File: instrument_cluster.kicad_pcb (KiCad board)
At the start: 2 copper layers, 99.1 x 45.7 mm, 80 parts, among them J1 Conn_02x16_Top_Bottom, J2 Conn_02x16_Top_Bottom, J3 USB mini-B SMD, J4 NOT_FITTED_SWD_Conn_01x04_Male, J5 54819-0572, J6 NOT_FITTED_SWD_Conn_01x04_Male, U1 LM2575S-5.0_NOPB, U10 74HC4050D, U11 TJA1040T, U12 TJA1040T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

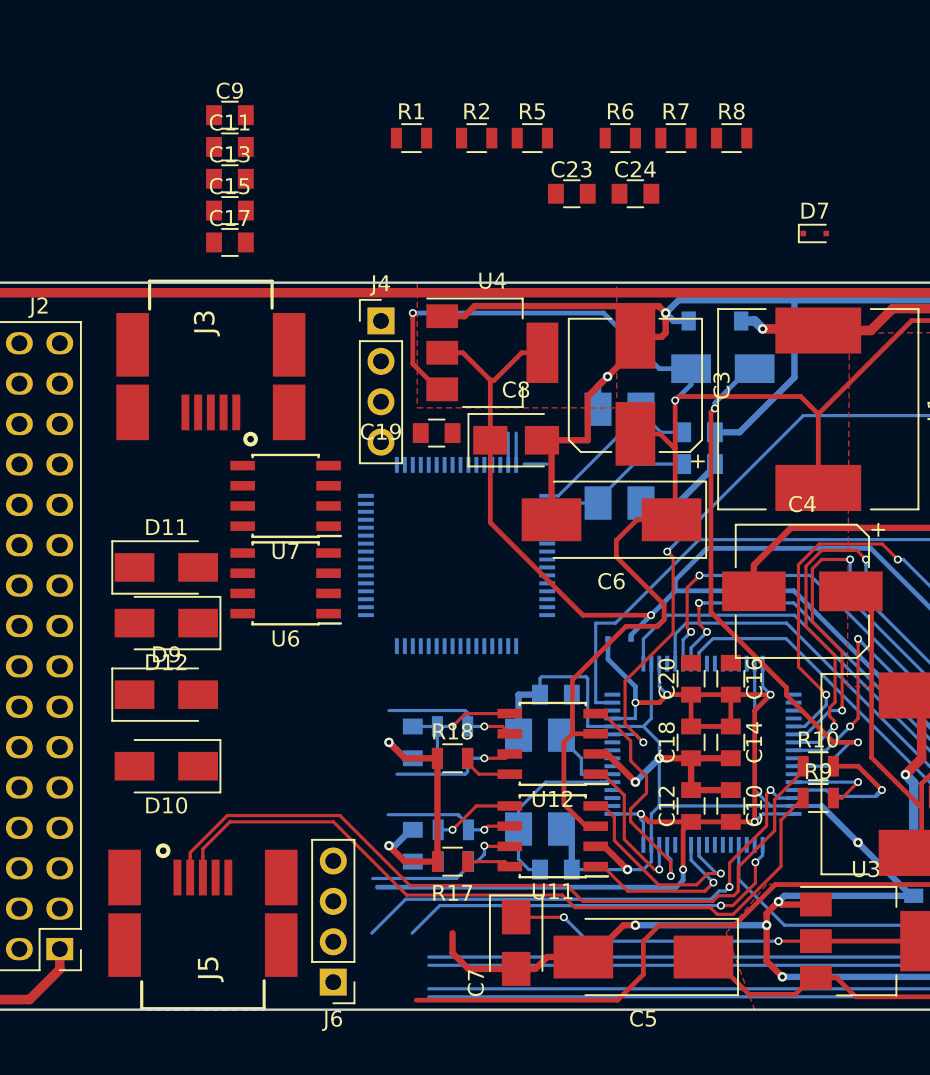
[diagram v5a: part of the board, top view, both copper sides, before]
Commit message: add resistor on can STB pin module A
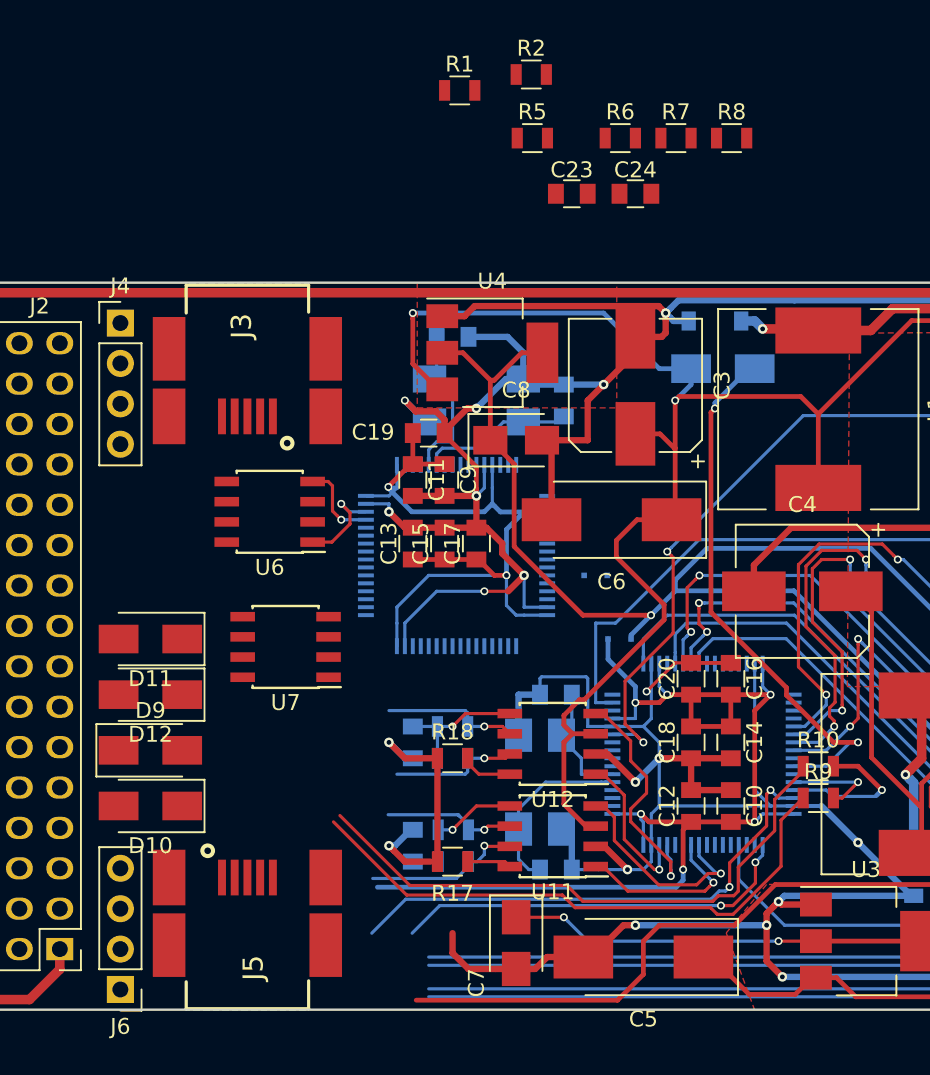
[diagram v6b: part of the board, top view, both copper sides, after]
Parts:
- D7: moved to B.Cu
- moved C9 26.6 mm to (138.5, 97.5), turned to 270 degrees
- moved C13 25.7 mm to (136.5, 101.5), turned to 90 degrees
- moved D7 25.5 mm to (148.0, 103.5)
- moved C15 24.9 mm to (138.5, 101.5), turned to 90 degrees
- moved C17 24.5 mm to (140.5, 101.5), turned to 90 degrees
- moved C11 23.9 mm to (136.5, 97.5), turned to 270 degrees
- moved C21 16.6 mm to (139.0, 88.5)
- moved J4 16.4 mm to (118.1, 87.6)
- moved J6 13.4 mm to (118.1, 129.5)
- moved Y1 9.66 mm to (140.5, 92.5), turned to 0 degrees
- moved U7 9.50 mm to (128.5, 108.0)
- moved C22 9.39 mm to (146.0, 92.5), turned to 90 degrees
- moved R2 5.27 mm to (143.9, 72.0)
- moved D11 4.61 mm to (120.0, 107.5), turned to 180 degrees
- moved D12 4.61 mm to (120.0, 111.0)
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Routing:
- net GND: track 402.9 -> 452.2 mm, vias 20 -> 27
- net /+3V3_STM-A: track 0.83 -> 49.6 mm, vias 0 -> 2
- net Net-(J5-Pad2): track 49.1 -> 37.1 mm
- net Net-(J5-Pad3): track 47.4 -> 36.7 mm
- net /Module A (2can_filter)/CAN1_TX: track 0.00 -> 6.07 mm, vias 0 -> 1
- net /Module A (2can_filter)/CAN1_RX: track 0.00 -> 5.27 mm, vias 0 -> 1
- net (no net): track 4.35 -> 0.00 mm
- net Net-(C22-Pad1): track 8.15 -> 9.87 mm
- net Net-(U5-Pad2): track 1.55 -> 0.00 mm
- net Net-(C21-Pad1): track 11.4 -> 10.1 mm
- net /+5V_CAN-B: track 99.9 -> 99.4 mm

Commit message: TODO swd module A, anti-theft
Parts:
- added R3: 10k, Resistors_SMD:R_0805, F.Cu at (121.0, 100.0)
- added R4: 10k, Resistors_SMD:R_0805, F.Cu at (130.5, 108.5)
- C23, C24, D10, D11, D12, D9, R5, R6, R7, R8: moved to B.Cu
- moved R8 42.1 mm to (127.0, 106.0), turned to 90 degrees
- moved R7 38.5 mm to (129.0, 106.0), turned to 270 degrees
- moved R2 37.1 mm to (137.5, 108.5), turned to 90 degrees
- moved C24 36.7 mm to (128.0, 108.5)
- moved R6 36.0 mm to (121.0, 98.0)
- moved R1 35.5 mm to (139.5, 108.5), turned to 90 degrees
- moved C23 34.1 mm to (118.5, 99.0), turned to 90 degrees
- moved R5 33.2 mm to (121.0, 100.0)
- moved U7 3.58 mm to (130.3, 104.9)
- moved R9 2.92 mm to (160.5, 120.0), turned to 90 degrees
- moved R10 2.24 mm to (160.0, 114.5)
- moved D10 1.00 mm to (120.0, 117.0)
- moved D11 1.00 mm to (120.0, 106.5), turned to 0 degrees
- moved D12 1.00 mm to (120.0, 110.0)
- moved D9 1.00 mm to (120.0, 113.5)
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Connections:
- U6 pad 8: GND -> Net-(R3-Pad1)
- U7 pad 8: GND -> Net-(R4-Pad1)
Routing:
- net GND: track 452.2 -> 582.7 mm, vias 27 -> 34
- net /USB_Vbus-A: track 41.2 -> 105.0 mm, vias 0 -> 2
- net /MS_CAN_H: track 74.9 -> 132.8 mm, vias 1 -> 6
- net /MS_CAN_L: track 81.5 -> 136.5 mm, vias 1 -> 7
- net /HS_CAN_H: track 73.6 -> 125.8 mm, vias 1 -> 6
- net /HS_CAN_L: track 72.9 -> 125.1 mm, vias 1 -> 6
- net /USB_Vbus-B: track 34.2 -> 81.4 mm, vias 2 -> 4
- net Net-(J3-Pad3): track 0.00 -> 28.3 mm, vias 0 -> 2
- net /ANTI-THEFT: track 17.6 -> 39.4 mm
- net Net-(J3-Pad2): track 0.00 -> 21.8 mm
- net /+3V3_STM-B: track 72.2 -> 91.6 mm
- net /Module B (2can_filter+extra)/SWCLK: track 25.5 -> 44.5 mm
- net /Module B (2can_filter+extra)/SWDIO: track 32.5 -> 49.7 mm
- net /+5V_CAN-A: track 143.0 -> 153.4 mm
- net Net-(C24-Pad2): track 0.00 -> 9.89 mm, vias 0 -> 1
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
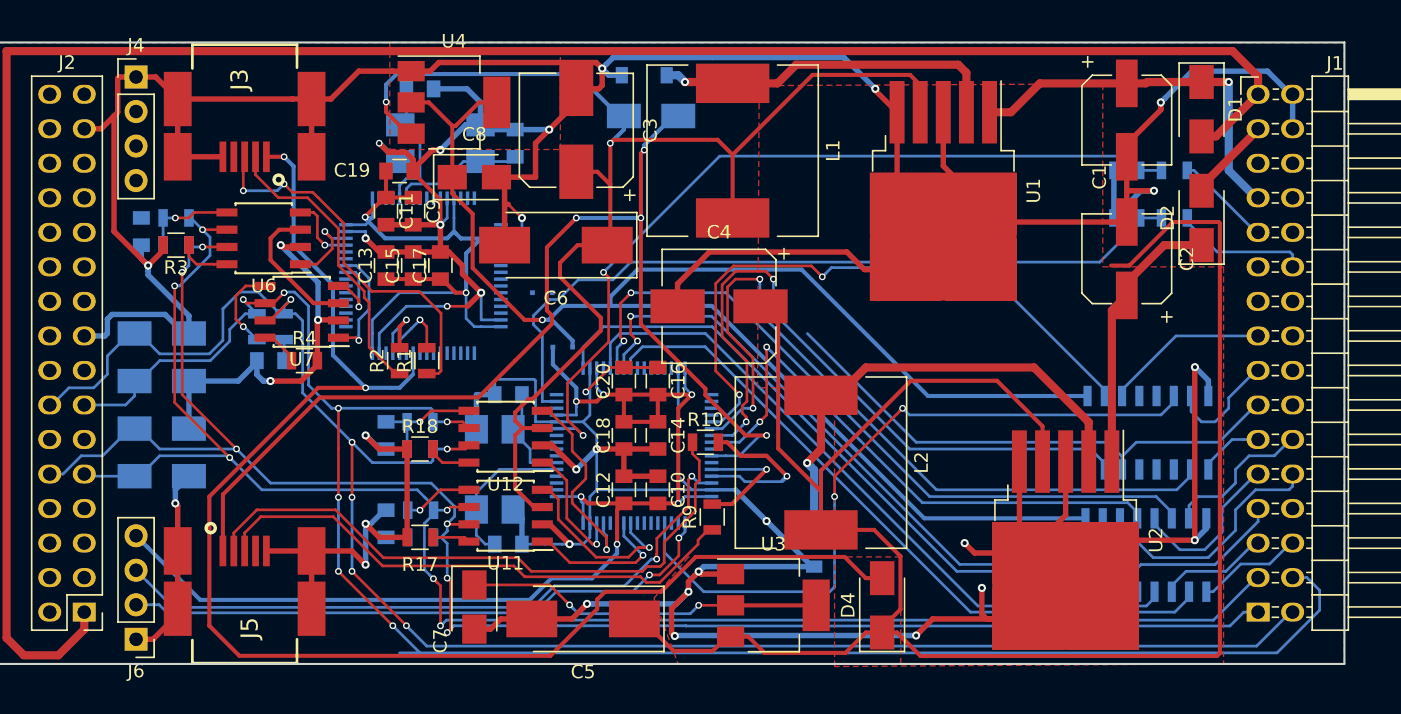
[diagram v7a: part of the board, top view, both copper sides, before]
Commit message: pcb tracing finish
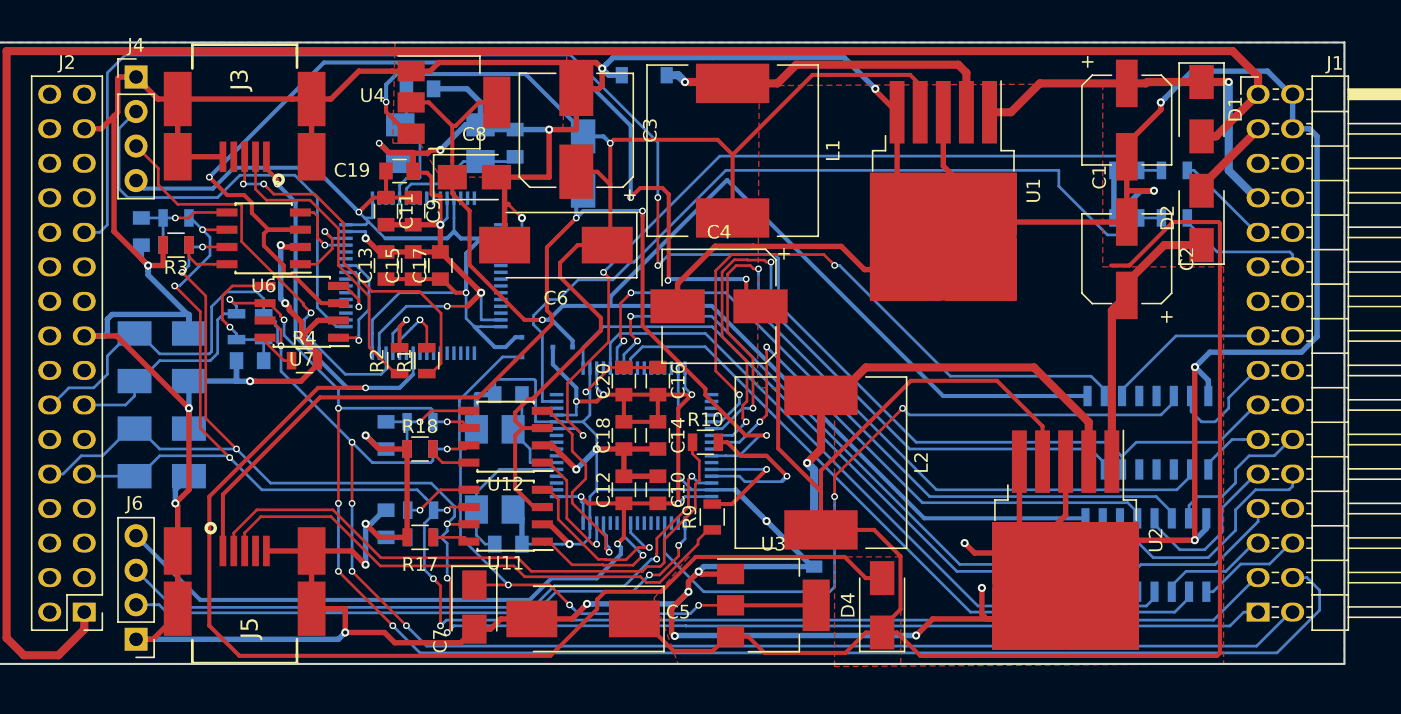
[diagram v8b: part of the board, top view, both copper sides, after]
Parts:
- moved D3 6.10 mm to (151.0, 94.0), turned to 270 degrees
- moved D7 4.27 mm to (146.5, 107.5), turned to 270 degrees
- moved C24 1.50 mm to (126.5, 108.5)
- moved R7 1.50 mm to (127.5, 106.0)
- moved R8 1.50 mm to (125.5, 106.0)
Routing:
- net GND: track 582.7 -> 665.1 mm, vias 34 -> 36
- net /ANTI-THEFT: track 39.4 -> 121.0 mm, vias 0 -> 2
- net /+5V_CAN-A: track 153.4 -> 222.6 mm, vias 0 -> 4
- net /Module A (2can_filter)/SWCLK: track 0.00 -> 33.2 mm
- net /Module A (2can_filter)/SWDIO: track 0.00 -> 30.6 mm, vias 0 -> 1
- net /+3V3_STM-A: track 49.6 -> 73.3 mm
- net Net-(C7-Pad1): track 26.3 -> 47.3 mm, vias 2 -> 3
- net /USB_Vbus-B: track 81.4 -> 75.6 mm, vias 4 -> 3
- net /+3V3_LSH-B: track 116.2 -> 121.6 mm
- net /Module B (2can_filter+extra)/stm_adc_1: track 57.0 -> 61.6 mm
- net /MS_CAN_L: track 136.5 -> 133.0 mm
- net /+5V_CAN-B: track 98.4 -> 96.0 mm
- net /Module B (2can_filter+extra)/anti-theft_stm: track 50.4 -> 52.2 mm
- net /Module B (2can_filter+extra)/belt: track 56.5 -> 58.2 mm
- net Net-(C23-Pad2): track 6.87 -> 8.47 mm
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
